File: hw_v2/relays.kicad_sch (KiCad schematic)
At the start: 24 parts, among them J10 Conn_01x01, J11 Conn_01x01, Q4 SS8050, Q5 SS8050, Q6 AO3400A, Q7 AO3400A, U18 VNLD5090, U5 TPL7407LAPWR

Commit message: WIP v7
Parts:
- added J2, J3: Conn_01x01, TestPoint:TestPoint_THTPad_2.0x2.0mm_Drill1.0mm, symbol Connector_Generic:Conn_01x01
- JP6, JP7, JP8: now fitted
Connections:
- net VVT-OUT: no longer names the net of U5.12 (OUT5), U5.13 (OUT4)
- net VVT-OUT: now also J3.1 (Pin_1)
- net vvt: no longer names the net of U5.4 (IN4), U5.5 (IN5)
- net vvt: now also J2.1 (Pin_1)
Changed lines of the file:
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@@
 (kicad_sch
-	(version 20240101)
+	(version 20241004)
 	(generator "eeschema")
 	(generator_version "8.99")
@@
 	)
 	(junction
+		(at 111.76 86.36)
+		(diameter 0)
+		(color 0 0 0 0)
+	)
+	(junction
 		(at 73.66 156.21)
 		(diameter 0)
@@
 	(wire
 		(pts
+			(xy 111.76 86.36) (xy 110.49 86.36)
+		)
+		(stroke
+			(width 0)
+			(type default)
+		)
+	)
+	(wire
+		(pts
 			(xy 86.36 92.71) (xy 85.09 92.71)
 		)
@@
 	(wire
 		(pts
-			(xy 113.03 86.36) (xy 110.49 86.36)
+			(xy 113.03 86.36) (xy 111.76 86.36)
 		)
 		(stroke
@@
 		)
 	)
-	(global_label "VVT-OUT"
-		(shape input)
-		(at 113.03 86.36 0)
-		(effects
-			(font
-				(size 1.27 1.27)
-			)
-			(justify left)
-		)
-		(property "Intersheetrefs" "${INTERSHEET_REFS}"
-			(at 113.03 86.36 0)
-			(effects
-				(font
-					(size 1.27 1.27)
-				)
-				(hide yes)
-			)
-		)
-	)
 	(global_label "FAN-OUT"
 		(shape input)
@@
 		(shape input)
 		(at 149.86 88.9 180)
-		(fields_autoplaced yes)
 		(effects
 			(font
@@
 		(shape input)
 		(at 86.36 77.47 180)
-		(fields_autoplaced yes)
 		(effects
 			(font
@@
 		(shape input)
 		(at 193.04 129.54 180)
-		(fields_autoplaced yes)
 		(effects
 			(font
@@
 		(shape input)
 		(at 83.82 163.83 180)
-		(fields_autoplaced yes)
 		(effects
 			(font
@@
 		(shape input)
 		(at 208.28 93.98 180)
-		(fields_autoplaced yes)
 		(effects
 			(font
@@
 		(shape input)
 		(at 86.36 82.55 180)
-		(fields_autoplaced yes)
 		(effects
 			(font
@@
 		(shape input)
 		(at 83.82 161.29 180)
-		(fields_autoplaced yes)
 		(effects
 			(font
@@
 		(shape input)
 		(at 86.36 80.01 180)
-		(fields_autoplaced yes)
-		(effects
-			(font
-				(size 1.27 1.27)
-			)
-			(justify right)
-		)
-	)
-	(hierarchical_label "vvt"
-		(shape input)
-		(at 83.82 86.36 180)
-		(fields_autoplaced yes)
 		(effects
 			(font
@@
 		(shape input)
 		(at 83.82 151.13 180)
-		(fields_autoplaced yes)
 		(effects
 			(font
@@
 		(shape input)
 		(at 193.04 137.16 180)
-		(fields_autoplaced yes)
 		(effects
 			(font
@@
 		(shape input)
 		(at 83.82 166.37 180)
-		(fields_autoplaced yes)
 		(effects
 			(font
@@
 		(in_bom no)
 		(on_board yes)
-		(dnp yes)
+		(dnp no)
 		(fields_autoplaced yes)
 		(property "Reference" "JP7"
@@
 		(in_bom no)
 		(on_board yes)
-		(dnp yes)
+		(dnp no)
 		(fields_autoplaced yes)
 		(property "Reference" "JP8"
@@
 		(in_bom no)
 		(on_board yes)
-		(dnp yes)
+		(dnp no)
 		(fields_autoplaced yes)
 		(property "Reference" "JP6"
@@
 	)
 	(symbol
+		(lib_id "Connector_Generic:Conn_01x01")
+		(at 116.84 86.36 0)
+		(unit 1)
+		(exclude_from_sim no)
+		(in_bom no)
+		(on_board yes)
+		(dnp yes)
+		(property "Reference" "J3"
+			(at 124.714 91.186 0)
+			(effects
+				(font
+					(size 1.27 1.27)
+				)
+			)
+		)
+		(property "Value" "Conn_01x01"
+			(at 126.492 88.392 0)
+			(effects
+				(font
+					(size 1.27 1.27)
+				)
+			)
+		)
+		(property "Footprint" "TestPoint:TestPoint_THTPad_2.0x2.0mm_Drill1.0mm"
+			(at 116.84 86.36 0)
+			(effects
+				(font
+					(size 1.27 1.27)
+				)
+				(hide yes)
+			)
+		)
+		(property "Datasheet" "~"
+			(at 116.84 86.36 0)
+			(effects
+				(font
+					(size 1.27 1.27)
+				)
+				(hide yes)
+			)
+		)
+		(property "Description" "Generic connector, single row, 01x01, script generated (kicad-library-utils/schlib/autogen/connector/)"
+			(at 116.84 86.36 0)
+			(effects
+				(font
+					(size 1.27 1.27)
+				)
+				(hide yes)
+			)
+		)
+		(pin "1"
+		)
+		(instances
+			(project "hw_v1"
+				(path "/b3feb07e-be80-40e1-bd13-6cd54c2f8b0c/aca74028-30ce-4304-a4a8-c39cedc5a58f"
+					(reference "J3")
+					(unit 1)
+				)
+			)
+		)
+	)
+	(symbol
 		(lib_id "power:GND")
 		(at 196.85 114.3 180)
@@
 					(unit 1)
 				)
+			)
+		)
+	)
+	(symbol
+		(lib_id "Connector_Generic:Conn_01x01")
+		(at 78.74 86.36 180)
+		(unit 1)
+		(exclude_from_sim no)
+		(in_bom no)
+		(on_board yes)
+		(dnp yes)
+		(property "Reference" "J2"
+			(at 70.866 81.534 0)
+			(effects
+				(font
+					(size 1.27 1.27)
+				)
+			)
+		)
+		(property "Value" "Conn_01x01"
+			(at 69.088 84.328 0)
+			(effects
+				(font
+					(size 1.27 1.27)
+				)
+			)
+		)
+		(property "Footprint" "TestPoint:TestPoint_THTPad_2.0x2.0mm_Drill1.0mm"
+			(at 78.74 86.36 0)
+			(effects
+				(font
+					(size 1.27 1.27)
+				)
+				(hide yes)
+			)
+		)
+		(property "Datasheet" "~"
+			(at 78.74 86.36 0)
+			(effects
+				(font
+					(size 1.27 1.27)
+				)
+				(hide yes)
+			)
+		)
+		(property "Description" "Generic connector, single row, 01x01, script generated (kicad-library-utils/schlib/autogen/connector/)"
+			(at 78.74 86.36 0)
+			(effects
+				(font
+					(size 1.27 1.27)
+				)
+				(hide yes)
+			)
+		)
+		(pin "1"
+		)
+		(instances
+			(project "hw_v1"
+				(path "/b3feb07e-be80-40e1-bd13-6cd54c2f8b0c/aca74028-30ce-4304-a4a8-c39cedc5a58f"
+					(reference "J2")
+					(unit 1)
+				)

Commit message: hw v2
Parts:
- removed D28: MM3Z24VT1G, Diode_SMD:D_SOD-323, symbol Device:D_Zener
- removed J10, J11, J2, J3: Conn_01x01, TestPoint:TestPoint_THTPad_2.0x2.0mm_Drill1.0mm, symbol Connector_Generic:Conn_01x01
- removed Q4, Q5: SS8050, Package_TO_SOT_SMD:SOT-23, symbol Transistor_BJT:2N3055
- removed Q6, Q7: AO3400A, Package_TO_SOT_SMD:SOT-23, symbol Transistor_FET:AO3400A
- removed R53, R68: 1k, Resistor_SMD:R_0603_1608Metric, symbol Device:R
- removed R54, R69: 100k, Resistor_SMD:R_0603_1608Metric, symbol Device:R
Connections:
- net CEL-OUT: now also U5.10 (OUT7), U5.11 (OUT6)
- net CEL_OUT: now also U5.6 (IN6), U5.7 (IN7)
- net RPM_OUT: now also U5.4 (IN4), U5.5 (IN5)
- net TACHO-OUT: now also U5.12 (OUT5), U5.13 (OUT4)
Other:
- note added: "Relay + tacometro + luz check"
- note removed: "TODO: estaria bueno agregarle un led a estas salidas"
- note removed: "Tachometer out"
- moved on the sheet: A1, C10, D29, D30, R55, R56, R57, R58, U18, U5

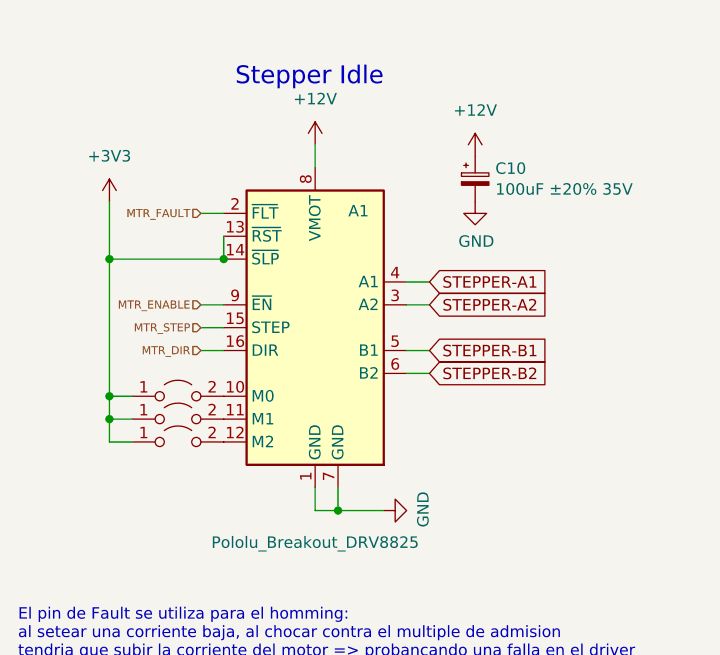
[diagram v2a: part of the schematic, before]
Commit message: fix LCSC codes
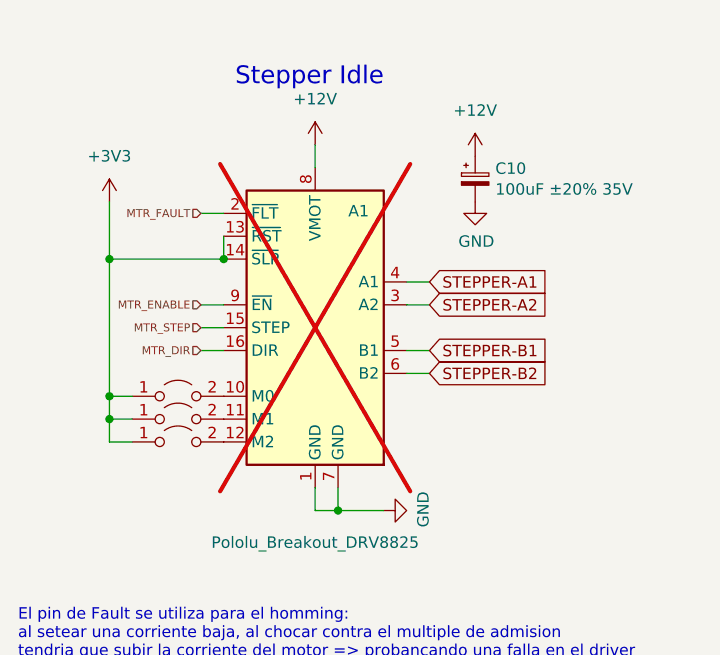
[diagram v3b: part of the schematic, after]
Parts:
- A1: now not fitted
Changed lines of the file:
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@@
 		(in_bom no)
 		(on_board yes)
-		(dnp no)
+		(dnp yes)
 		(property "Reference" "A1"
 			(at 79.756 124.206 0)

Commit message: Fix some ERC errors
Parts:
- C10: symbol Device:CP_Small -> Device:C_Polarized_Small
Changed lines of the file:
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@@
 			)
 		)
-		(property "Description" ""
+		(property "Description" "Power symbol creates a global label with name \"GND\" , ground"
 			(at 82.55 157.48 0)
 			(effects
@@
 			)
 		)
-		(property "Description" ""
+		(property "Description" "Power symbol creates a global label with name \"GND\" , ground"
 			(at 59.69 93.98 0)
 			(effects
@@
 			)
 		)
-		(property "Description" ""
+		(property "Description" "Power symbol creates a global label with name \"GND\" , ground"
 			(at 227.33 121.92 0)
 			(effects
@@
 	)
 	(symbol
-		(lib_id "Device:CP_Small")
+		(lib_id "Device:C_Polarized_Small")
 		(at 92.71 120.65 0)
 		(unit 1)
@@
 			)
 		)
-		(property "Description" ""
+		(property "Description" "Polarized capacitor, small symbol"
 			(at 92.71 120.65 0)
 			(effects
@@
 			)
 		)
-		(property "Description" ""
+		(property "Description" "Power symbol creates a global label with name \"GND\" , ground"
 			(at 92.71 123.19 0)
 			(effects
@@
 			)
 		)
-		(property "Description" ""
+		(property "Description" "Power symbol creates a global label with name \"GND\" , ground"
 			(at 227.33 129.54 0)
 			(effects
@@
 			)
 		)
-		(property "Description" ""
+		(property "Description" "Power symbol creates a global label with name \"GND\" , ground"
 			(at 184.15 102.87 0)
 			(effects
@@
 			)
 		)
-		(property "Description" ""
+		(property "Description" "Power symbol creates a global label with name \"GND\" , ground"
 			(at 184.15 140.97 0)
 			(effects

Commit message: planito mas catolico
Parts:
- removed U18: VNLD5090, Package_SO:SOIC-8_3.9x4.9mm_P1.27mm, symbol v0.4.4d-rescue:VNLD5090-IC_Automotive-v0.4.4c-rescue
- removed U5: TPL7407LAPWR, Package_SO:TSSOP-16_4.4x5mm_P0.65mm, symbol OpenEFI-STM32-rev3:TPL7407LAPWR
- added U5: ~, symbol hw_v2:VNLD5090
- added U9: TPL7407LAPWR || ULN2003A, symbol Transistor_Array:ULN2003A
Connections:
- net +12V: now also U9.9 (COM)
- net BOOST-OUT: now also U5.6 (DRAIN2)
- net CEL-OUT: now also U9.10 (O7), U9.11 (O6)
- net CEL_OUT: now also U9.6 (I6), U9.7 (I7)
- net FAN-OUT: now also U9.15 (O2)
- net FAN2-OUT: now also U9.14 (O3)
- net FUELPUMP-OUT: now also U9.16 (O1)
- net GND: now also U5.5 (SOURCE2), U5.7 (SOURCE1), U9.8 (GND)
- net IDLE-OUT: now also U5.8 (DRAIN1)
- net RPM_OUT: now also U9.4 (I4), U9.5 (I5)
- net TACHO-OUT: now also U9.12 (O5), U9.13 (O4)
- net fan1: now also U9.2 (I2)
- net fan2: now also U9.3 (I3)
- net fuel_pump: now also U9.1 (I1)
- net at R57.2: now also U5.1 (IN1)
- net at R58.1: now also U5.3 (IN2)
- no-connect marks 0 -> 2

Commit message: wip CKP/CMP
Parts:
- U5: footprint (none) -> Package_SO:SO-8_3.9x4.9mm_P1.27mm
- U9: footprint (none) -> Package_SO:TSSOP-16_4.4x5mm_P0.65mm
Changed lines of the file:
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@@
 (kicad_sch
-	(version 20241004)
+	(version 20241209)
 	(generator "eeschema")
 	(generator_version "8.99")
@@
 			)
 		)
-		(property "Footprint" ""
+		(property "Footprint" "Package_SO:SO-8_3.9x4.9mm_P1.27mm"
 			(at 213.36 111.76 0)
 			(effects
@@
 			)
 		)
-		(property "Footprint" ""
+		(property "Footprint" "Package_SO:TSSOP-16_4.4x5mm_P0.65mm"
 			(at 74.93 87.63 0)
 			(effects

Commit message: update ADC oamp
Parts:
- C10: LCSC C141427 -> C3339
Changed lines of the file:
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@@
 			)
 		)
-		(property "LCSC" "C141427"
+		(property "LCSC" "C3339"
 			(at 92.71 120.65 0)
 			(effects
